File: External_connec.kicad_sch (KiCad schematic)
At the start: 16 parts, among them CN1 JST_Battery, J11 CAN_TX, J12 CAN_RX, J13 Conn_01x08, J14 Conn_01x06, J15 Conn_01x10, J16 Conn_01x08, J2 A - B, J21 U2U, J3 H - L, J4 TYPE-C-31-M12_13, J5 EXT_LOAD, J9 Conn_01x06

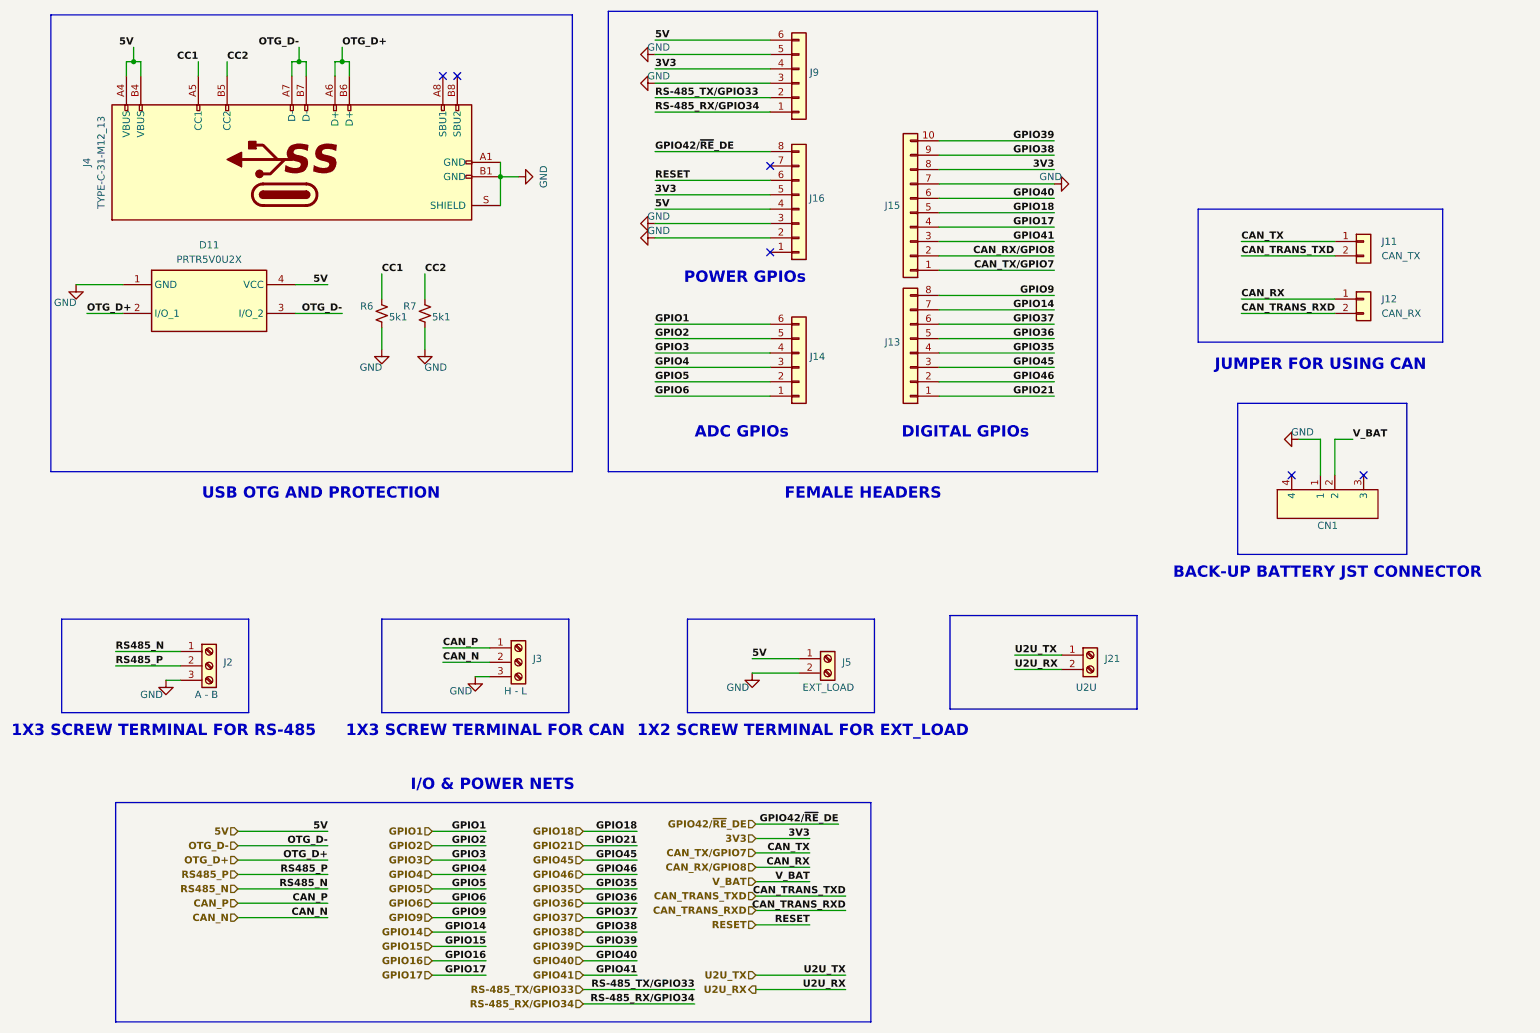
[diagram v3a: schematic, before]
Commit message: Added selection jumper block diagram and solved DRC errors
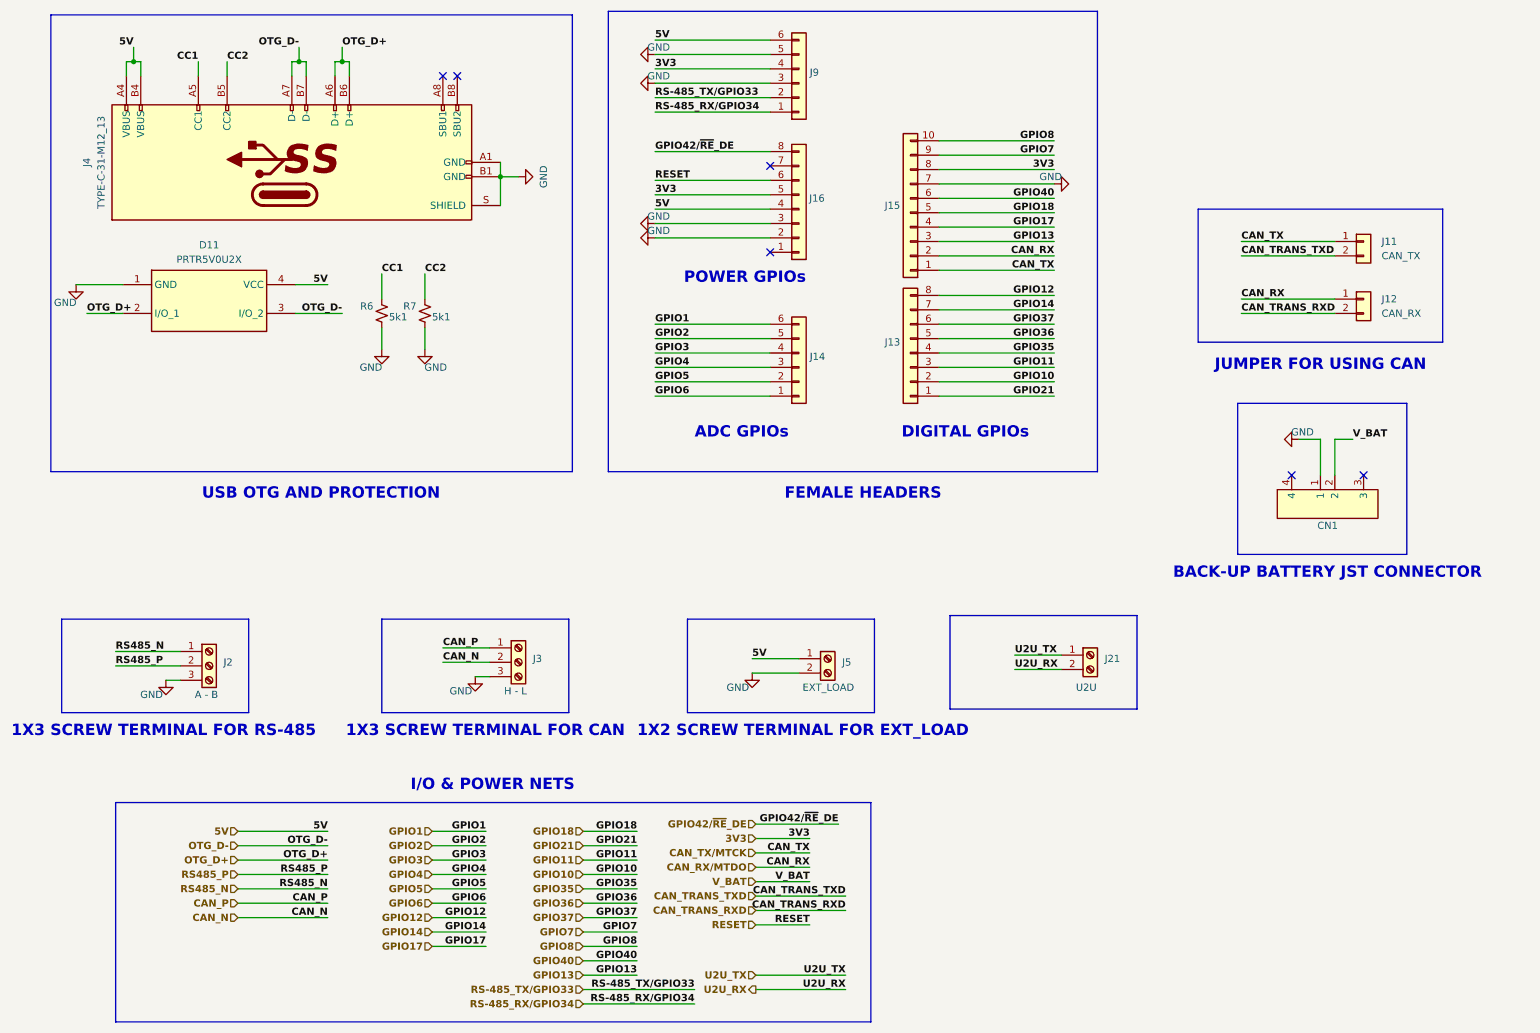
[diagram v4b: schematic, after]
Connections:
- net CAN_RX/GPIO8 renamed CAN_RX/MTDO
- net CAN_TX/GPIO7 renamed CAN_TX/MTCK
- net GPIO38 renamed GPIO7
- net GPIO39 renamed GPIO8
- net GPIO41 renamed GPIO13
- net GPIO45 renamed GPIO11
- net GPIO46 renamed GPIO10
- net GPIO9 renamed GPIO12

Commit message: Added HW-Tinkerers logo and supporting graphics
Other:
- company: (none) -> HW-TINKERERS (hw.tinkerers@gmail.com)
- title: (none) -> HARDWARE TINKERERS ESP32-S3 DB
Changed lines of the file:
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@@
 (kicad_sch (version 20230121) (generator eeschema)
   (paper "A4")
+  (title_block
+    (title "HARDWARE TINKERERS ESP32-S3 DB")
+    (rev "1.0.0")
+    (company "HW-TINKERERS (hw.tinkerers@gmail.com)")
+    (comment 1 "Email: bhandarkasrishtikr111@gmail.com")
+    (comment 2 "Author: Srishtik Bhandarkar")
+    (comment 3 "Email: vaibhavkhatri00@gmail.com")
+    (comment 4 "Author: Vaibhav Khatri")
+    (comment 5 "Official HW-Tinkerers email: hw.tinkerers@gmail.com")
+  )
   (junction (at 99.695 45.72) (diameter 0) (color 0 0 0 0)
   )

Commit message: Added production files for JLC (BOM and CPL)
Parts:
- CN1: LCSC Part Number (none) -> C295747
- D11: LCSC Part Number (none) -> C2827688
- J11, J12, J13, J14, J15, J16, J2, J21, J3, J5, J9: now left out of the parts list
- R6, R7: LCSC Part Number (none) -> C105872
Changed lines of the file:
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@@
+      (effects (font (size 1.27 1.27)) hide)
+    )
+    (property "LCSC Part Number" "C2827688" (at 33.02 64.77 0)
       (effects (font (size 1.27 1.27)) hide)
     )
@@
   )
   (symbol (lib_id "ESP32-S3_DB:Conn_01x02") (at 252.095 57.15 0) (unit 1)
-    (in_bom yes) (on_board yes) (dnp no) (fields_autoplaced)
+    (in_bom no) (on_board yes) (dnp no) (fields_autoplaced)
     (property "Reference" "J11" (at 255.27 57.15 0)
       (effects (font (size 1.27 1.27)) (justify left))
@@
       (effects (font (size 1.27 1.27)) hide)
     )
+    (property "Sim.Enable" "0" (at 252.095 57.15 0)
+      (effects (font (size 1.27 1.27)) hide)
+    )
     (pin "1")
     (pin "2")
@@
     )
     (property "PN" "RC0402FR-075K1L" (at 78.74 69.85 0)
+      (effects (font (size 1.27 1.27)) hide)
+    )
+    (property "LCSC Part Number" "C105872" (at 78.74 69.85 0)
       (effects (font (size 1.27 1.27)) hide)
     )
@@
   )
   (symbol (lib_id "ESP32-S3_DB:Conn_01x06") (at 152.4 29.21 0) (mirror x) (unit 1)
-    (in_bom yes) (on_board yes) (dnp no)
+    (in_bom no) (on_board yes) (dnp no)
     (property "Reference" "J9" (at 154.305 27.305 0)
       (effects (font (size 1.27 1.27)) (justify left))
@@
     )
     (property "Datasheet" "~" (at 152.4 29.21 0)
+      (effects (font (size 1.27 1.27)) hide)
+    )
+    (property "Sim.Enable" "0" (at 152.4 29.21 0)
       (effects (font (size 1.27 1.27)) hide)
     )
@@
   )
   (symbol (lib_id "ESP32-S3_DB:Screw_Terminal_01x02") (at 157.48 130.81 0) (unit 1)
-    (in_bom yes) (on_board yes) (dnp no)
+    (in_bom no) (on_board yes) (dnp no)
     (property "Reference" "J5" (at 160.02 131.445 0)
       (effects (font (size 1.27 1.27)) (justify left))
@@
       (effects (font (size 1.27 1.27)) hide)
     )
+    (property "Sim.Enable" "0" (at 157.48 130.81 0)
+      (effects (font (size 1.27 1.27)) hide)
+    )
     (pin "1")
     (pin "2")
@@
       (effects (font (size 1.27 1.27)) hide)
     )
+    (property "LCSC Part Number" "C105872" (at 86.36 69.85 0)
+      (effects (font (size 1.27 1.27)) hide)
+    )
     (pin "1")
     (pin "2")
@@
   )
   (symbol (lib_id "ESP32-S3_DB:Conn_01x02") (at 252.095 67.31 0) (unit 1)
-    (in_bom yes) (on_board yes) (dnp no) (fields_autoplaced)
+    (in_bom no) (on_board yes) (dnp no) (fields_autoplaced)
     (property "Reference" "J12" (at 255.27 67.31 0)
       (effects (font (size 1.27 1.27)) (justify left))
@@
       (effects (font (size 1.27 1.27)) hide)
     )
+    (property "Sim.Enable" "0" (at 252.095 67.31 0)
+      (effects (font (size 1.27 1.27)) hide)
+    )
     (pin "1")
     (pin "2")
@@
     )
     (property "PN" "S2B-PH-SM4-TB(LF)(SN) " (at 245.745 102.235 0)
+      (effects (font (size 1.27 1.27)) hide)
+    )
+    (property "LCSC Part Number" "C295747" (at 245.745 102.235 0)
       (effects (font (size 1.27 1.27)) hide)
     )
@@
   )
   (symbol (lib_id "ESP32-S3_DB:Conn_01x08") (at 172.085 76.835 180) (unit 1)
-    (in_bom yes) (on_board yes) (dnp no)
+    (in_bom no) (on_board yes) (dnp no)
     (property "Reference" "J13" (at 168.91 74.93 0)
       (effects (font (size 1.27 1.27)))
@@
     )
     (property "Datasheet" "~" (at 172.085 76.835 0)
+      (effects (font (size 1.27 1.27)) hide)
+    )
+    (property "Sim.Enable" "0" (at 172.085 76.835 0)
       (effects (font (size 1.27 1.27)) hide)
     )
@@
   )
   (symbol (lib_id "ESP32-S3_DB:Conn_01x06") (at 152.4 79.375 0) (mirror x) (unit 1)
-    (in_bom yes) (on_board yes) (dnp no)
+    (in_bom no) (on_board yes) (dnp no)
     (property "Reference" "J14" (at 154.305 77.47 0)
       (effects (font (size 1.27 1.27)) (justify left))
@@
     )
     (property "Datasheet" "~" (at 152.4 79.375 0)
+      (effects (font (size 1.27 1.27)) hide)
+    )
+    (property "Sim.Enable" "0" (at 152.4 79.375 0)
       (effects (font (size 1.27 1.27)) hide)
     )
@@
   )
   (symbol (lib_id "ESP32-S3_DB:Screw_Terminal_01x02") (at 203.835 130.175 0) (unit 1)
-    (in_bom yes) (on_board yes) (dnp no)
+    (in_bom no) (on_board yes) (dnp no)
     (property "Reference" "J21" (at 206.375 130.81 0)
       (effects (font (size 1.27 1.27)) (justify left))
@@
       (effects (font (size 1.27 1.27)) hide)
     )
+    (property "Sim.Enable" "0" (at 203.835 130.175 0)
+      (effects (font (size 1.27 1.27)) hide)
+    )
     (pin "1")
     (pin "2")
@@
   )
   (symbol (lib_id "ESP32-S3_DB:Conn_01x08") (at 152.4 51.435 0) (mirror x) (unit 1)
-    (in_bom yes) (on_board yes) (dnp no)
+    (in_bom no) (on_board yes) (dnp no)
     (property "Reference" "J16" (at 155.575 49.53 0)
       (effects (font (size 1.27 1.27)))
@@
     )
     (property "Datasheet" "~" (at 152.4 51.435 0)
+      (effects (font (size 1.27 1.27)) hide)
+    )
+    (property "Sim.Enable" "0" (at 152.4 51.435 0)
       (effects (font (size 1.27 1.27)) hide)
     )
@@
   )
   (symbol (lib_id "ESP32-S3_DB:Screw_Terminal_01x03") (at 48.26 132.08 0) (unit 1)
-    (in_bom yes) (on_board yes) (dnp no)
+    (in_bom no) (on_board yes) (dnp no)
     (property "Reference" "J2" (at 50.8 131.445 0)
       (effects (font (size 1.27 1.27)) (justify left))
@@
     )
     (property "PN" "" (at 48.26 132.08 0)
+      (effects (font (size 1.27 1.27)) hide)
+    )
+    (property "Sim.Enable" "0" (at 48.26 132.08 0)
       (effects (font (size 1.27 1.27)) hide)
     )
@@
   )
   (symbol (lib_id "ESP32-S3_DB:Conn_01x10") (at 172.085 52.07 180) (unit 1)
-    (in_bom yes) (on_board yes) (dnp no)
+    (in_bom no) (on_board yes) (dnp no)
     (property "Reference" "J15" (at 168.91 50.8 0)
       (effects (font (size 1.27 1.27)))
@@
     )
     (property "Datasheet" "~" (at 172.085 52.07 0)
+      (effects (font (size 1.27 1.27)) hide)
+    )
+    (property "Sim.Enable" "0" (at 172.085 52.07 0)
       (effects (font (size 1.27 1.27)) hide)
     )
@@
   )
   (symbol (lib_id "ESP32-S3_DB:Screw_Terminal_01x03") (at 102.87 131.445 0) (unit 1)
-    (in_bom yes) (on_board yes) (dnp no)
+    (in_bom no) (on_board yes) (dnp no)
     (property "Reference" "J3" (at 105.41 130.81 0)
       (effects (font (size 1.27 1.27)) (justify left))
@@
       (effects (font (size 1.27 1.27)) hide)
     )
+    (property "Sim.Enable" "0" (at 102.87 131.445 0)
+      (effects (font (size 1.27 1.27)) hide)
+    )
